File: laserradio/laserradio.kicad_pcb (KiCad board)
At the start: 2 copper layers, 24 x 51.9 mm, 35 parts, among them J1 USB4105-GF-A, J2 LEFT, J3 DEBUG, J4 RIGHT, U1 W25Q128JV, U2 RP2040, U3 MCP1702T-3302E_CB, Y1 12MHz

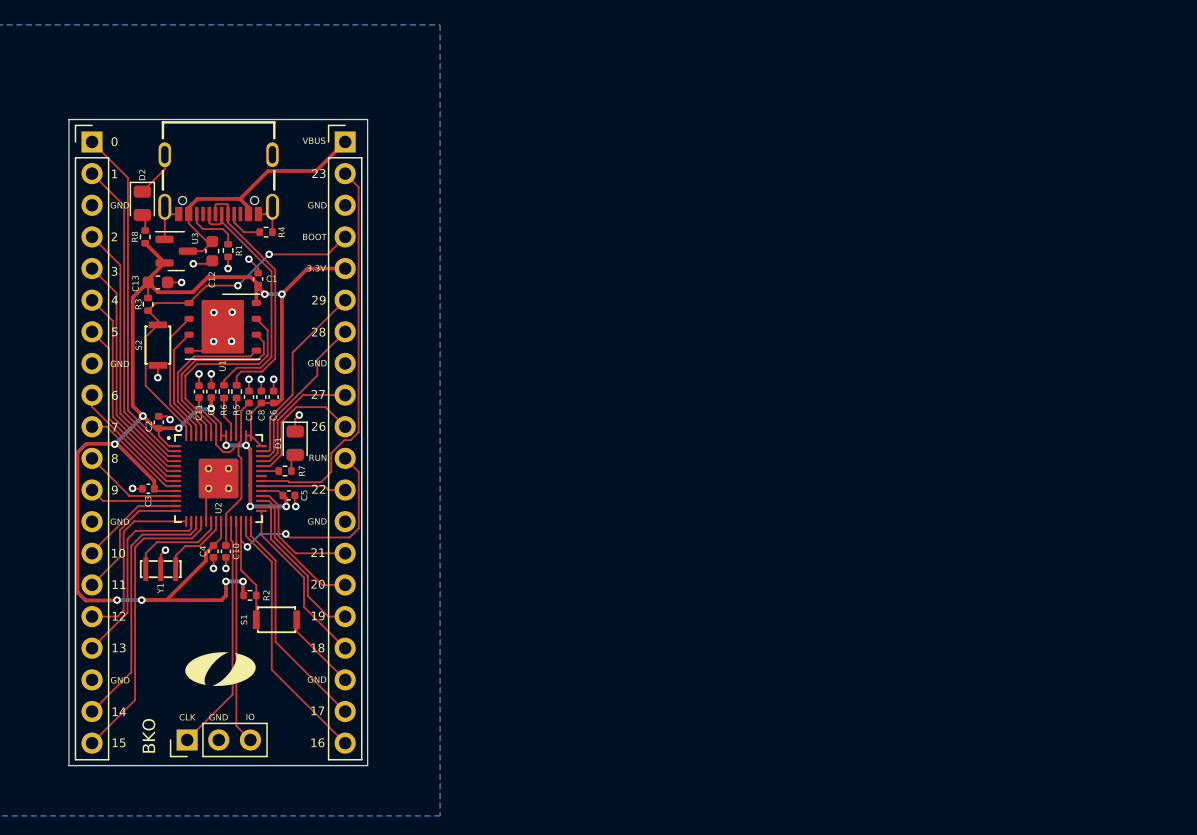
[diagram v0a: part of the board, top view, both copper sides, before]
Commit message: Updated PCB file from schematic
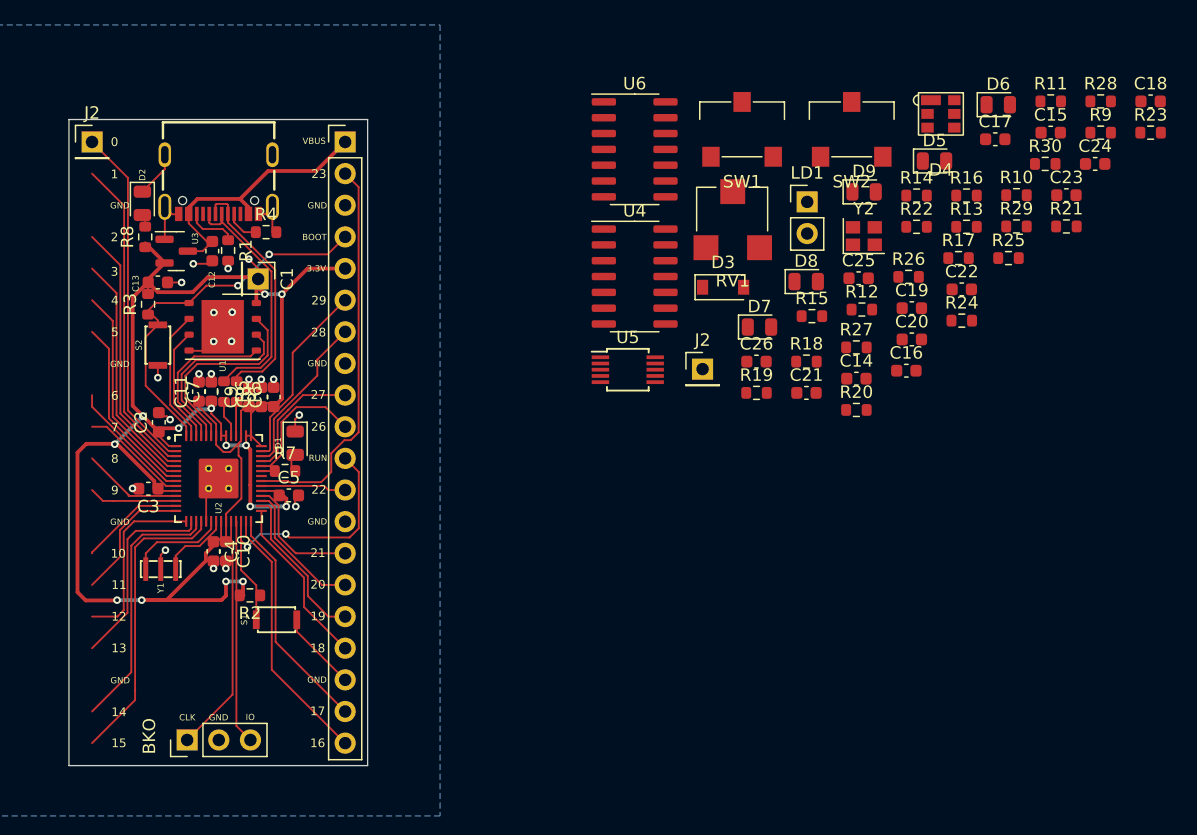
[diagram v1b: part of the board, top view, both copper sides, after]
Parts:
- removed OlinLogo: G***, Eclectronics:OlinLogo
- added C14: 10µF, Capacitor_SMD:C_0603_1608Metric, F.Cu at (165.5, 91.9)
- added C15: 10pF, Capacitor_SMD:C_0603_1608Metric, F.Cu at (181.1, 72.2)
- added C16: 10µF, Capacitor_SMD:C_0603_1608Metric, F.Cu at (169.5, 91.3)
- added C17: 10pF, Capacitor_SMD:C_0603_1608Metric, F.Cu at (176.7, 72.7)
- added C18: 10pF, Capacitor_SMD:C_0603_1608Metric, F.Cu at (189.1, 69.6)
- added C19: 10µF, Capacitor_SMD:C_0603_1608Metric, F.Cu at (169.9, 86.2)
- added C20: 1pF, Capacitor_SMD:C_0603_1608Metric, F.Cu at (169.9, 88.8)
- added C21: 10pF, Capacitor_SMD:C_0603_1608Metric, F.Cu at (161.5, 93.0)
- added C22: 10pF, Capacitor_SMD:C_0603_1608Metric, F.Cu at (174.0, 84.7)
- added C23: 10µF, Capacitor_SMD:C_0603_1608Metric, F.Cu at (182.4, 77.2)
- added C24: 10pF, Capacitor_SMD:C_0603_1608Metric, F.Cu at (184.7, 74.7)
- added C25: 10µF, Capacitor_SMD:C_0603_1608Metric, F.Cu at (165.7, 83.8)
- added C26: 10µF, Capacitor_SMD:C_0603_1608Metric, F.Cu at (157.5, 90.5)
- added D3: DIODE, Diode_SMD:D_SOD-123, F.Cu at (154.8, 84.6)
- added D4: D_Photo, Eclectronics:Photodiode, F.Cu at (172.3, 70.6)
- added D5: LED, LED_SMD:LED_0805_2012Metric, F.Cu at (171.8, 74.4)
- added D6: LED, LED_SMD:LED_0805_2012Metric, F.Cu at (176.9, 69.9)
- added D7: LED, LED_SMD:LED_0805_2012Metric, F.Cu at (157.7, 87.8)
- added D8: LED, LED_SMD:LED_0805_2012Metric, F.Cu at (161.5, 84.1)
- added D9: LED, LED_SMD:LED_0805_2012Metric, F.Cu at (166.1, 76.9)
- added J2: Conn_01x01_Female, Connector_PinHeader_2.54mm:PinHeader_1x01_P2.54mm_Vertical, F.Cu at (153.2, 91.1)
- added LD1: D_Laser_1A3C, Connector_PinHeader_2.54mm:PinHeader_1x02_P2.54mm_Vertical, F.Cu at (161.6, 77.7)
- added R10: 330k, Resistor_SMD:R_0603_1608Metric, F.Cu at (178.3, 77.2)
- added R11: 1K, Resistor_SMD:R_0603_1608Metric, F.Cu at (181.1, 69.6)
- added R12: 3.3k, Resistor_SMD:R_0603_1608Metric, F.Cu at (165.9, 86.3)
- added R13: 1k, Resistor_SMD:R_0603_1608Metric, F.Cu at (174.3, 79.7)
- added R14: 3.3k, Resistor_SMD:R_0603_1608Metric, F.Cu at (170.3, 77.2)
- added R15: 10k, Resistor_SMD:R_0603_1608Metric, F.Cu at (161.9, 86.9)
- added R16: 100k, Resistor_SMD:R_0603_1608Metric, F.Cu at (174.3, 77.2)
- added R17: 1k, Resistor_SMD:R_0603_1608Metric, F.Cu at (173.7, 82.2)
- added R18: 1K, Resistor_SMD:R_0603_1608Metric, F.Cu at (161.5, 90.5)
- added R19: 5k, Resistor_SMD:R_0603_1608Metric, F.Cu at (157.5, 93.0)
- added R20: 10k, Resistor_SMD:R_0603_1608Metric, F.Cu at (165.5, 94.4)
- added R21: 1K, Resistor_SMD:R_0603_1608Metric, F.Cu at (182.4, 79.7)
- added R22: 1K, Resistor_SMD:R_0603_1608Metric, F.Cu at (170.3, 79.7)
- added R23: 1K, Resistor_SMD:R_0603_1608Metric, F.Cu at (189.1, 72.2)
- added R24: 1.2k, Resistor_SMD:R_0603_1608Metric, F.Cu at (174.0, 87.2)
- added R25: 3.3k, Resistor_SMD:R_0603_1608Metric, F.Cu at (177.7, 82.2)
- added R26: 3.3k, Resistor_SMD:R_0603_1608Metric, F.Cu at (169.7, 83.7)
- added R27: 3.3k, Resistor_SMD:R_0603_1608Metric, F.Cu at (165.5, 89.4)
- added R28: 3.3k, Resistor_SMD:R_0603_1608Metric, F.Cu at (185.1, 69.6)
- added R29: 3.3k, Resistor_SMD:R_0603_1608Metric, F.Cu at (178.3, 79.7)
- added R30: 3.3k, Resistor_SMD:R_0603_1608Metric, F.Cu at (180.7, 74.7)
- added R9: 100k, Resistor_SMD:R_0603_1608Metric, F.Cu at (185.1, 72.2)
- added RV1: Nominal 10k, Eclectronics:Laser Potentiometer, F.Cu at (155.6, 79.1)
- added SW1: SW_SPDT, Eclectronics:Laser Switch, F.Cu at (156.3, 71.9)
- added SW2: SW_SPDT, Eclectronics:Laser Switch, F.Cu at (165.1, 71.9)
- added U4: ADA4891, Package_SO:SOIC-14_3.9x8.7mm_P1.27mm, F.Cu at (147.7, 83.7)
- added U5: RS2255, Package_SO:MSOP-10_3x3mm_P0.5mm, F.Cu at (147.2, 91.2)
- added U6: ADA4891, Package_SO:SOIC-14_3.9x8.7mm_P1.27mm, F.Cu at (147.7, 73.5)
- added Y2: ASE-xxxMHz, Crystal:Crystal_SMD_2520-4Pin_2.5x2.0mm, F.Cu at (166.1, 80.5)
- C1: footprint Capacitor_SMD:C_0402_1005Metric -> Connector_PinHeader_2.54mm:PinHeader_1x01_P2.54mm_Vertical
- C10, C11, C2, C3, C4, C5, C6, C7, C8, C9: footprint Capacitor_SMD:C_0402_1005Metric -> Capacitor_SMD:C_0603_1608Metric
- J2: value LEFT -> Conn_01x01_Female; footprint Connector_PinHeader_2.54mm:PinHeader_1x20_P2.54mm_Vertical -> Connector_PinHeader_2.54mm:PinHeader_1x01_P2.54mm_Vertical
- R1, R2, R3, R4, R5, R6, R7, R8: footprint Resistor_SMD:R_0402_1005Metric -> Resistor_SMD:R_0603_1608Metric
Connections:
- J2 pad 1: /GPIO0 -> Net-(J2-Pad1)
- J4 pad 1: /VBUS -> /BOOT
- J4 pad 10: /GPIO26 -> /GPIO24
- J4 pad 11: /RUN -> /GPIO23
- J4 pad 13: GND -> /GPIO21
- J4 pad 14: /GPIO21 -> /GPIO20
- J4 pad 15: /GPIO20 -> /GPIO19
- J4 pad 16: /GPIO19 -> /GPIO18
- J4 pad 17: /GPIO18 -> /GPIO17
- J4 pad 18: GND -> /GPIO16
- J4 pad 19: /GPIO17 -> GND
- J4 pad 2: /GPIO23 -> /VBUS
- J4 pad 20: /GPIO16 -> /RUN
- J4 pad 4: /BOOT -> +3V3
- J4 pad 5: +3V3 -> /GPIO29
- J4 pad 6: /GPIO29 -> /GPIO28
- J4 pad 7: /GPIO28 -> /GPIO27
- J4 pad 8: GND -> /GPIO26
- J4 pad 9: /GPIO27 -> GND
- U2 pad 2: /GPIO0 -> /Rx
- U2 pad 3: /GPIO1 -> /Tx
- U2 pad 4: /GPIO2 -> /Tx_ENABLE
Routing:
- net +3V3: track 128.5 -> 323.9 mm, vias 14 -> 19
- net /VBUS: track 23.1 -> 54.7 mm
- net /GPIO23: track 31.6 -> 0.00 mm
- net /BOOT: track 30.4 -> 0.00 mm, vias 2 -> 0
- net /GPIO0: track 27.9 -> 0.00 mm
- net GND: track 42.1 -> 70.0 mm, vias 21 -> 18
- net /Tx: track 0.00 -> 25.8 mm
- net /GPIO1: track 25.8 -> 0.00 mm
- net Net-(J1-PadA6): track 21.2 -> 0.00 mm
- net /Tx_ENABLE: track 0.00 -> 21.2 mm
- net /GPIO2: track 21.2 -> 0.00 mm
- net /RUN: track 26.5 -> 47.6 mm
- net /GPIO16: track 21.1 -> 0.00 mm
- net Net-(C10-Pad1): track 19.4 -> 0.00 mm
- net /SWCLK: track 19.1 -> 0.00 mm
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
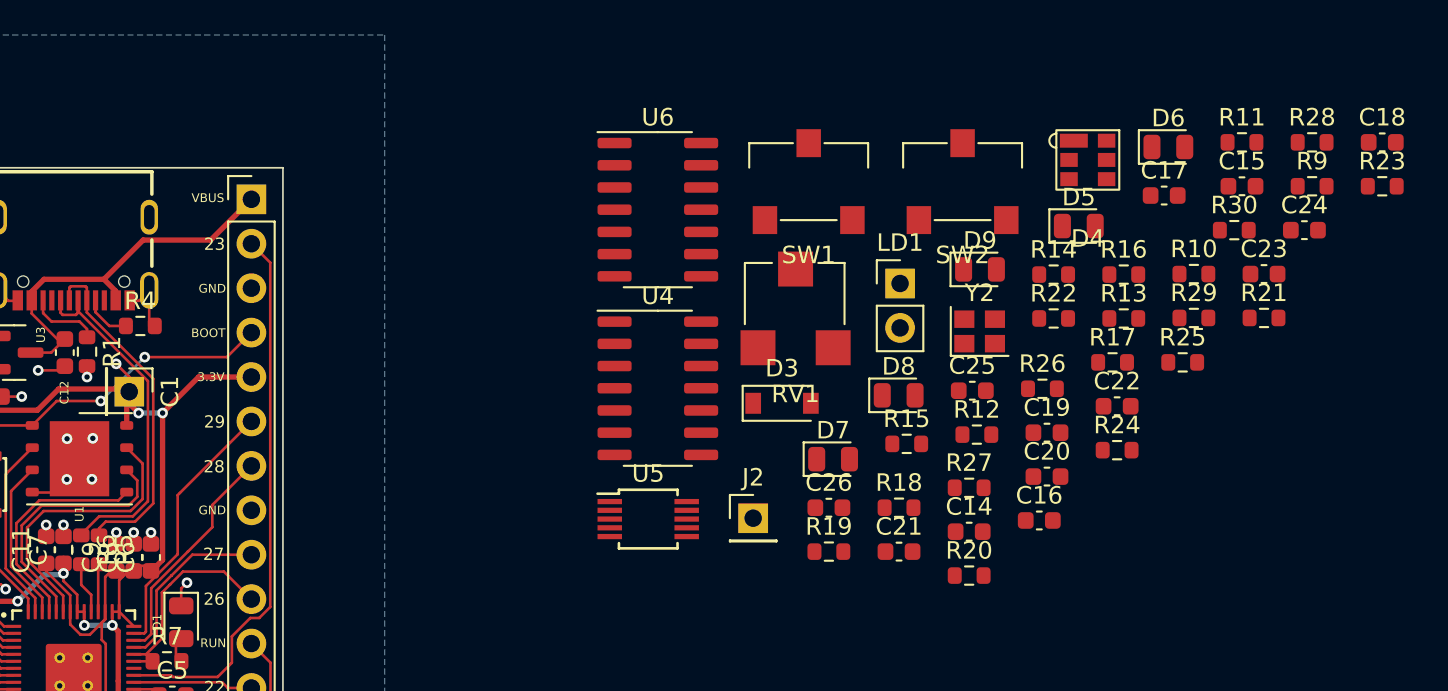
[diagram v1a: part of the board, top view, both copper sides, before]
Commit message: Fixed schematic bugs
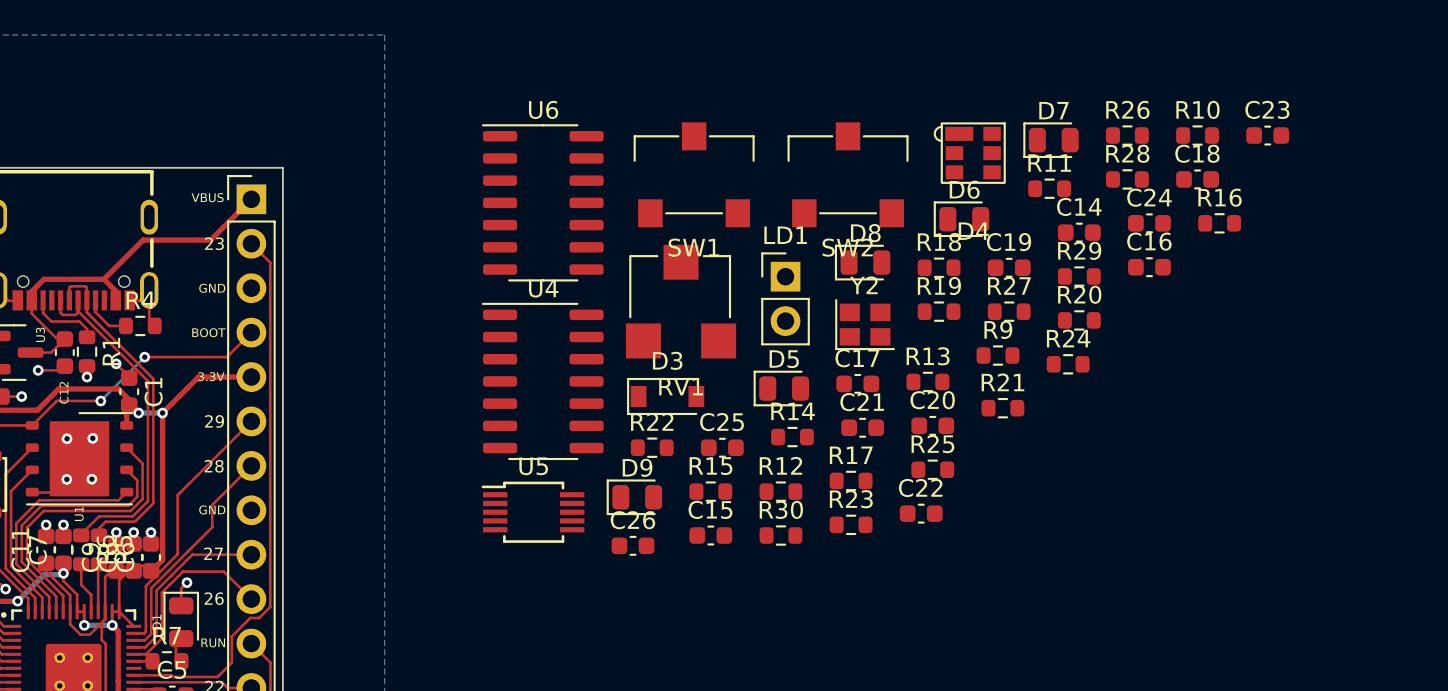
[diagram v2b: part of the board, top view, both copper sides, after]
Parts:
- removed the J2 at (153.2, 91.1)
- C1: footprint Connector_PinHeader_2.54mm:PinHeader_1x01_P2.54mm_Vertical -> Capacitor_SMD:C_0603_1608Metric
- moved C15 36.3 mm to (150.7, 92.1)
- moved R23 36.0 mm to (158.8, 91.5)
- moved R30 31.3 mm to (154.7, 92.1)
- moved R22 24.1 mm to (147.4, 87.1)
- moved D9 23.5 mm to (146.5, 89.9)
- moved D7 22.2 mm to (170.3, 69.5)
- moved C17 20.6 mm to (159.1, 83.5)
- moved R9 20.4 mm to (167.2, 81.8)
- moved D5 19.2 mm to (154.9, 83.7)
- moved C14 18.2 mm to (171.8, 74.8)
- moved R14 17.6 mm to (155.4, 86.5)
- moved R17 16.4 mm to (158.8, 89.0)
- moved R20 15.9 mm to (171.8, 79.8)
- moved R21 15.8 mm to (167.4, 84.8)
- moved C16 15.8 mm to (175.8, 76.8)
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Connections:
- LD1 pad 2: (no net) -> Net-(LD1-Pad2)
- R17 pad 2: Net-(LD1-Pad3) -> Net-(LD1-Pad2)
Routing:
- net +3V3: track 323.9 -> 270.9 mm, vias 19 -> 16
- net /BOOT: track 0.00 -> 30.4 mm, vias 0 -> 2
- net Net-(J1-PadA6): track 0.00 -> 21.2 mm
- net /RUN: track 47.6 -> 26.5 mm
- net /GPIO16: track 0.00 -> 21.1 mm
- net /GPIO19: track 11.0 -> 23.7 mm
- net /GPIO18: track 12.8 -> 0.00 mm
- net GND: track 70.0 -> 71.5 mm, vias 18 -> 19

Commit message: Fixed unconnected capacitor
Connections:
- C21 pad 1: unconnected-(C21-Pad1) -> Net-(D3-Pad2)
- C21 pad 2: unconnected-(C21-Pad2) -> GND
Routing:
- net GND: track 71.5 -> 33.9 mm
- net /VBUS: track 54.7 -> 23.1 mm
- net /GPIO23: track 0.00 -> 31.6 mm
- net /GPIO18: track 0.00 -> 13.8 mm
- net /GPIO28: track 0.00 -> 13.1 mm
- net /GPIO20: track 0.00 -> 11.0 mm
- net /GPIO19: track 23.7 -> 12.8 mm
- net /GPIO16: track 21.1 -> 27.5 mm
- net /GPIO17: track 13.8 -> 18.4 mm

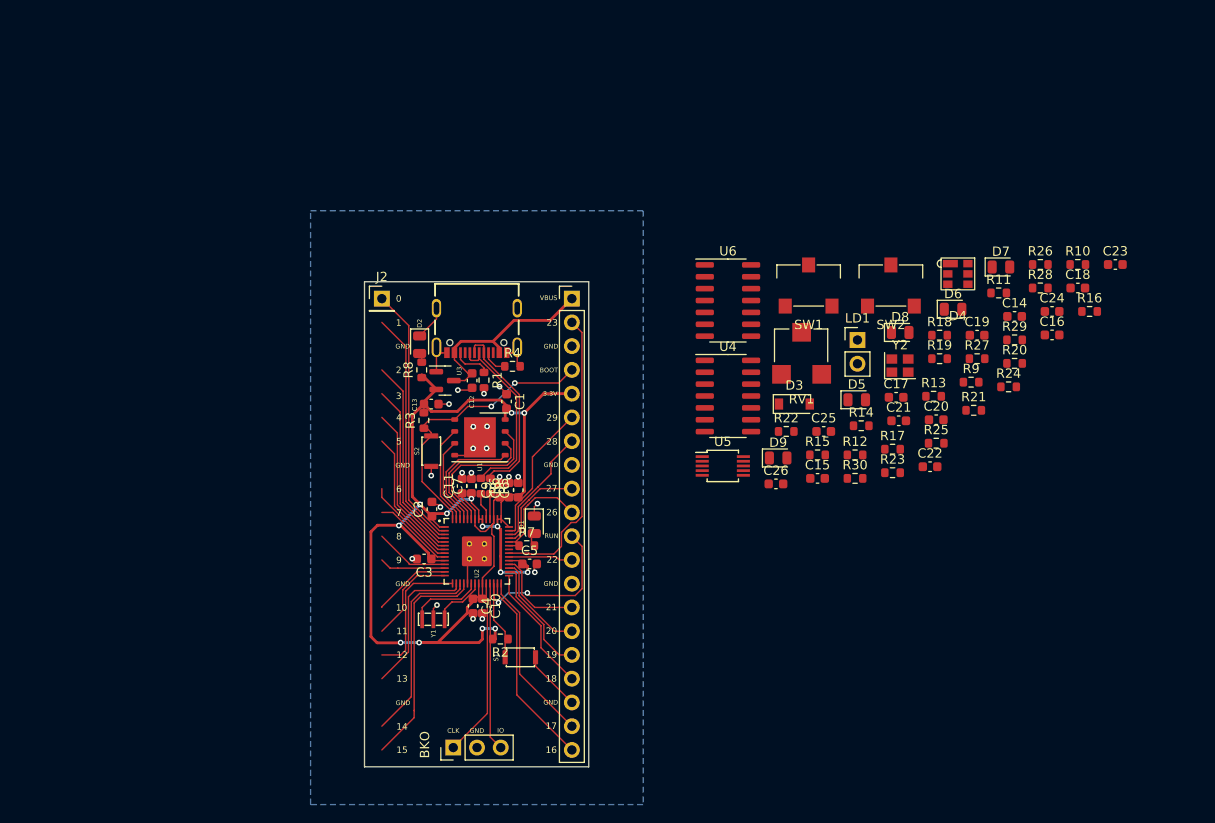
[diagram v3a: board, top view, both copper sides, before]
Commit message: start layout of op-amp units
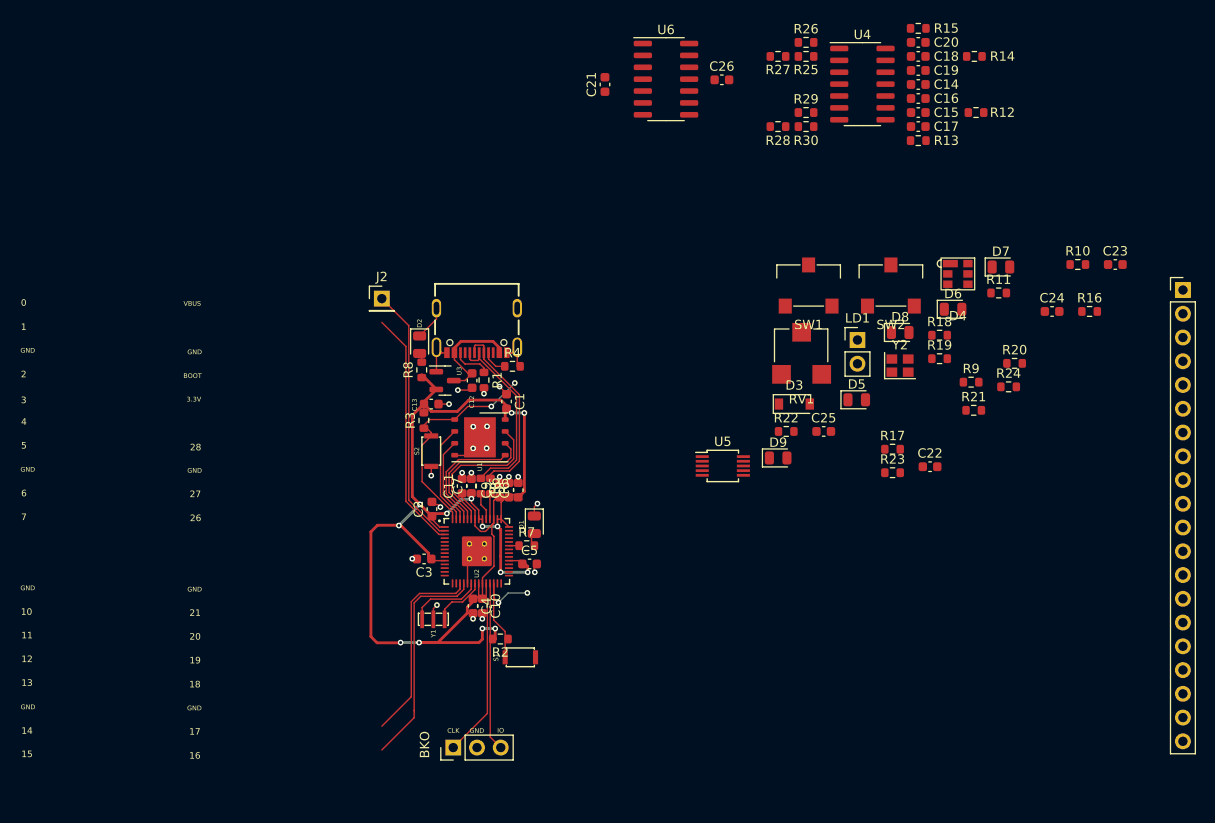
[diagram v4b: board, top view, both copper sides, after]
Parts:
- moved J4 65.3 mm to (189.8, 72.0)
- moved C21 47.7 mm to (128.0, 50.0), turned to 90 degrees
- moved R15 46.9 mm to (161.5, 44.0), turned to 180 degrees
- moved R25 43.6 mm to (149.5, 47.0), turned to 180 degrees
- moved C26 43.6 mm to (140.5, 49.5)
- moved R14 41.3 mm to (167.5, 47.0), turned to 180 degrees
- moved C15 40.6 mm to (161.5, 53.0), turned to 180 degrees
- moved C20 40.4 mm to (161.5, 45.5), turned to 180 degrees
- moved R12 38.8 mm to (167.7, 53.0)
- moved R27 38.7 mm to (146.5, 47.0), turned to 180 degrees
- moved R30 38.0 mm to (149.5, 54.5)
- moved U4 36.3 mm to (155.5, 50.0)
- moved R26 34.5 mm to (149.5, 45.5)
- moved R29 33.0 mm to (149.5, 53.0)
- moved R28 32.9 mm to (146.5, 54.5)
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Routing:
- net +3V3: track 270.9 -> 230.9 mm
- net /GPIO23: track 31.6 -> 0.00 mm
- net /GPIO16: track 27.5 -> 0.00 mm
- net /Tx_ENABLE: track 21.2 -> 0.00 mm
- net /GPIO3: track 19.0 -> 0.00 mm
- net /GPIO17: track 18.4 -> 0.00 mm
- net /GPIO4: track 16.9 -> 0.00 mm
- net /GPIO13: track 16.0 -> 0.00 mm
- net /GPIO5: track 14.8 -> 0.00 mm
- net /GPIO12: track 14.4 -> 0.00 mm
- net /GPIO18: track 13.8 -> 0.00 mm
- net /GPIO28: track 13.1 -> 0.00 mm
- net /GPIO19: track 12.8 -> 0.00 mm
- net /GPIO27: track 12.7 -> 0.00 mm
- net /RUN: track 26.5 -> 14.2 mm
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- removed copper zone on B.Cu, net GND
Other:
- board outline removed
- board text removed: "22"
- board text removed: "23"
- board text removed: "29"
- board text removed: "8"
- board text removed: "9"
- board text removed: "RUN"
